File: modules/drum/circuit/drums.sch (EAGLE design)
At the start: 43 parts, among them IC1 LM324N, IC2 LM324N, Q1 2N3904

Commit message: a few misc changes
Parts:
- added 10K_POT5, 10K_POT6, 10K_POT7, HH_TRIGGER, WOODBLOCK_TRIGGER: (no value), pinhead:PINHD-1X2
- added 1M: 1M, SparkFun-Resistors:100KOHM-HORIZ-1/4W-5%
- added C10, C9: 6800pF, capacitor-wima:C5/3
- added C11: 10uF, rcl:CPOL-USTT5D11
- added C12: 0.1uF, capacitor-wima:C5/3
- added C13, C14: 100pF, capacitor-wima:C5/3
- added C15: 4.7nF, capacitor-wima:C5/3
- added C16, C17: 300pF, capacitor-wima:C5/3
- added D3, D4, D5: 1A/50V/1.1V, SparkFun-DiscreteSemi:DIODE-KIT2
- added FTDI: (no value), pinhead:PINHD-1X6
- added JP1: (no value), pinhead:PINHD-1X4
- added Q2: 2N3904, transistor-small-signal:2N3904
- added R22: 100k, SparkFun-Resistors:100KOHM-HORIZ-1/4W-5%
- added R23, R27: 1k, SparkFun-Resistors:100KOHM-HORIZ-1/4W-5%
- added R24: 2M, SparkFun-Resistors:100KOHM-HORIZ-1/4W-5%
- added R25: 10k, SparkFun-Resistors:100KOHM-HORIZ-1/4W-5%
- added R26, R28, R29, R36: 100, SparkFun-Resistors:100KOHM-HORIZ-1/4W-5%
- added R30, R37: 100K, SparkFun-Resistors:100KOHM-HORIZ-1/4W-5%
- added R31: 50K, SparkFun-Resistors:100KOHM-HORIZ-1/4W-5%
- added R32: 3.6K, SparkFun-Resistors:100KOHM-HORIZ-1/4W-5%
- added R33: 10K, SparkFun-Resistors:100KOHM-HORIZ-1/4W-5%
- added R34, R35: 220K, SparkFun-Resistors:100KOHM-HORIZ-1/4W-5%
- C4: value 10uF -> 0.1uF
- R10: value 50K -> 100K
- R9: value 100K -> 50K
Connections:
- removed net N$15: IC1B.-IN, R10.2, R9.1
- removed net N$5: C3.2, IC1A.OUT, R10.1, R3.2, R5.2
- new net +12V: JP1.1
- new net -5V: IC1P.V-, IC2P.V-
- new net HH_OUT: C17.2, IC1D.OUT, R35.1, R37.1
- new net N$25: D3.A, WOODBLOCK_TRIGGER.2
- new net N$26: D3.C, R22.1
- new net N$27: IC1C.+IN, R22.2, R23.2
- new net N$29: 10K_POT5.1, C10.1, C9.2, R27.2
- new net N$30: C9.1, IC1C.-IN, R24.1
- new net N$31: 10K_POT5.2, R27.1, R28.2
- new net N$32: D4.A, HH_TRIGGER.2
- new net N$33: C11.+, D4.C, R26.2
- new net N$34: IC2C.+IN, R10.2, R30.1, R31.2, R37.2, R9.2
- new net N$35: 10K_POT6.1, R26.1
- new net N$36: 10K_POT6.2, C15.1, D5.A
- new net N$37: C4.2, NOISE_CHIP.(PCINT11/~RESET/DW)PB3, R25.1
- new net N$38: D5.C, Q2.C
- new net N$39: C12.1, R32.1
- new net N$40: 1M.2, C12.2, C13.2, Q2.B
- new net N$41: HH_TRIGGER.1, R29.2
- new net N$42: C13.1, R33.1
- new net N$43: C15.2, R34.2
- new net N$44: C14.2, R32.2
- new net N$45: 10K_POT7.1, R36.2
- new net N$46: C16.2, C17.1, R36.1
- new net N$48: C16.1, IC1D.-IN, R34.1, R35.2
- new net OUT: IC2C.OUT, JP1.4, R30.2
- new net RESET: C4.1, FTDI.6
- new net RX: FTDI.5, NOISE_CHIP.(PCINT1/AIN0/ADC1)PA1
- new net TX: FTDI.4, NOISE_CHIP.(PCINT2/AIN1/ADC2)PA2
- new net WB_OUT: C10.2, IC1C.OUT, R24.2, R9.1
- net +5V: now also 1M.1, IC1P.V+, IC2P.V+, R25.2, R29.1, WOODBLOCK_TRIGGER.1
- net BD_OUT: now also C3.2, IC1A.OUT, R3.2, R31.1, R5.2; no longer IC1B.OUT, R9.2
- net GND: now also 10K_POT7.2, C11.-, FTDI.1, IC1D.+IN, IC2C.-IN, JP1.3, Q2.E, R23.1, R28.1; no longer IC1B.+IN
- net METALIC: now also C14.1
- net NOISE: now also R33.2
- net SNARE_OUT: now also R10.1
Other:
- moved on the sheet: 10K_POT, 10K_POT1, 10K_POT2, 10K_POT3, BD_TRIGGER, IC1A, IC1C, IC1D, IC2A, IC2B, IC2C, IC2D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

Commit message: Drums
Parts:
- removed METAL_POT: metal_pot, pinhead:PINHD-1X3
- added 1M1, 1M2: 220, SparkFun-Resistors:100KOHM-HORIZ-1/4W-5%
- added C18, C19, C20: 100nF, capacitor-wima:C5/3
- added D6: 1A/50V/1.1V, SparkFun-DiscreteSemi:DIODE-KIT2
- added OK1: 6N138, optocoupler:6N138
- added R38, R39, R41, R42, R43, R44, R45: 100k, SparkFun-Resistors:100KOHM-HORIZ-1/4W-5%
- added R40: 10k, SparkFun-Resistors:100KOHM-HORIZ-1/4W-5%
- R11: value 100k -> 100
- R12, R23: value 1k -> 100k
- R19: value 100K -> 100k
- R2: value 1k -> 10k
- R20: value 50K -> 100k
- R21: value 100K -> 100
- R22: value 100k -> 10k
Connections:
- removed net N$1: METAL_POT.2, NOISE_CHIP.(PCINT5/OC1B/MISO/DO/ADC5)PA5
- removed net N$13: IC2A.+IN, R11.2, R12.2
- removed net N$14: C7.2, IC2A.OUT, R13.2, R15.2, R20.1
- removed net N$21: IC2B.-IN, R19.1, R20.2
- removed net N$8: D2.A, SNARE_TRIGGER.2
- new net BD_TRIGGER: NOISE_CHIP.(PCINT8/XTAL1/CLKI)PB0, R12.2
- new net DIN5_4: 1M2.2
- new net DIN5_5: D2.A, OK1.C
- new net HH_TRIGGER: NOISE_CHIP.(PCINT10/INT0/OC0A/CKOUT)PB2, R11.2
- new net MIDI_RX: 1M1.1, NOISE_CHIP.(PCINT6/OC1A/SDA/MOSI/ADC6)PA6, OK1.VO
- new net N$15: C19.1, R19.1, R42.2, WOODBLOCK_TRIGGER.2
- new net N$28: D6.C, IC1C.+IN, R40.2
- new net N$47: R41.2, WOODBLOCK_TRIGGER.1
- new net N$49: C19.2, D6.A, R43.2
- new net N$5: BD_TRIGGER.1, R38.2
- new net N$50: C20.2, D3.A, R45.2
- new net SNARE_TRIGGER: NOISE_CHIP.(PCINT0/AREF/ADC0)PA0, R20.2
- new net WB_TRIGGER: NOISE_CHIP.(PCINT9/XTAL2)PB1, R19.2
- net +5V: now also 1M1.2, OK1.VCC, R23.1, R38.1, R41.1; no longer BD_TRIGGER.1, METAL_POT.1, SNARE_TRIGGER.1, WOODBLOCK_TRIGGER.1
- net BD_OUT: now also C7.2, IC2A.OUT, R13.2, R15.2; no longer IC2B.OUT, R19.2
- net GND: now also OK1.GND, R1.1, R22.1, R39.1, R40.1, R42.1, R43.1, R44.1, R45.1; no longer IC2B.+IN, METAL_POT.3, R12.1, R23.1
- net N$12: now also 1M2.1, OK1.A; no longer R11.1
- net N$2: now also C18.1, R12.1, R39.2; no longer D1.A
- net N$25: now also C20.1, R20.1, R44.2, SNARE_TRIGGER.2; no longer D3.A, WOODBLOCK_TRIGGER.2
- net N$26: now also IC2A.+IN, R22.2; no longer R22.1
- net N$27: now also SNARE_TRIGGER.1; no longer IC1C.+IN, R22.2
- net N$3: now also IC1A.+IN, R2.2; no longer R1.1
- net N$32: now also R11.1
- net N$4: now also C18.2, D1.A; no longer IC1A.+IN, R2.2
- net NOISE: now also NOISE_CHIP.(PCINT5/OC1B/MISO/DO/ADC5)PA5; no longer NOISE_CHIP.(PCINT6/OC1A/SDA/MOSI/ADC6)PA6
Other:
- moved on the sheet: BD_TRIGGER, SNARE_TRIGGER, WOODBLOCK_TRIGGER

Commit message: drum board
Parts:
- added 10K_POT8, 10K_POT9, CLING_TRIGGER: (no value), pinhead:PINHD-1X2
- added 1M3, 1M4, R49: 1k, SparkFun-Resistors:100KOHM-HORIZ-1/4W-5%
- added C21, C22, C24, C26, C28: 100nF, capacitor-wima:C5/3
- added C23: 10uF, rcl:CPOL-USTT5D11
- added C25, C27: 330nF, capacitor-wima:C5/3
- added D7, D8: 1A/50V/1.1V, SparkFun-DiscreteSemi:DIODE-KIT2
- added IC3: 7905, linear:7905T
- added IC4: 7805T, adafruit:7805T
- added Q3: 2N3904, transistor-small-signal:2N3904
- added R46: 1M, SparkFun-Resistors:100KOHM-HORIZ-1/4W-5%
- added R47, R48: 47K, SparkFun-Resistors:100KOHM-HORIZ-1/4W-5%
- added R50: 100, SparkFun-Resistors:100KOHM-HORIZ-1/4W-5%
- added R51: 2.2K, SparkFun-Resistors:100KOHM-HORIZ-1/4W-5%
- added R52, R54, R55, R56, R57: 100k, SparkFun-Resistors:100KOHM-HORIZ-1/4W-5%
- added R53, R59: 10k, SparkFun-Resistors:100KOHM-HORIZ-1/4W-5%
- added R58: 100K, SparkFun-Resistors:100KOHM-HORIZ-1/4W-5%
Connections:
- new net 10K_POT3: 10K_POT9.1, R47.1, R48.1
- new net BD_OUT1: C22.2, IC2B.OUT, R46.2, R48.2, R59.2
- new net CLING_OUT: IC1B.-IN, IC1B.OUT, R58.1
- new net CLING_TRIGGER: NOISE_CHIP.(PCINT3/T0/ADC3)PA3, R57.2
- new net GND2: 1M4.1, C27.1, IC3.VI, JP1.3
- new net N$1: 10K_POT8.1, C21.2, C22.1, R49.2
- new net N$13: 10K_POT8.2, R49.1, R50.2
- new net N$14: 10K_POT9.2, R51.1
- new net N$21: C23.+, R51.2
- new net N$51: Q3.B, R52.2
- new net N$52: D8.C, Q3.C
- new net N$53: D8.A, IC1B.+IN, R59.1
- new net N$54: C24.1, CLING_TRIGGER.2, R55.2, R57.1
- new net N$55: D7.C, IC2B.+IN, R53.2
- new net N$56: CLING_TRIGGER.1, R54.2
- new net N$57: C24.2, D7.A, R56.2
- new net N$8: C21.1, IC2B.-IN, R46.1, R47.2
- net +12V: now also 1M3.2, C25.2, IC4.VI
- net +5V: now also C26.2, IC4.VO, R54.1
- net -5V: now also C28.1, IC3.VO
- net GND: now also 1M3.1, 1M4.2, C23.-, C25.1, C26.1, C27.2, C28.2, IC3.GND, IC4.GND, Q3.E, R50.1, R53.1, R55.1, R56.1; no longer JP1.3
- net METALIC: now also R52.1
- net N$34: now also R58.2

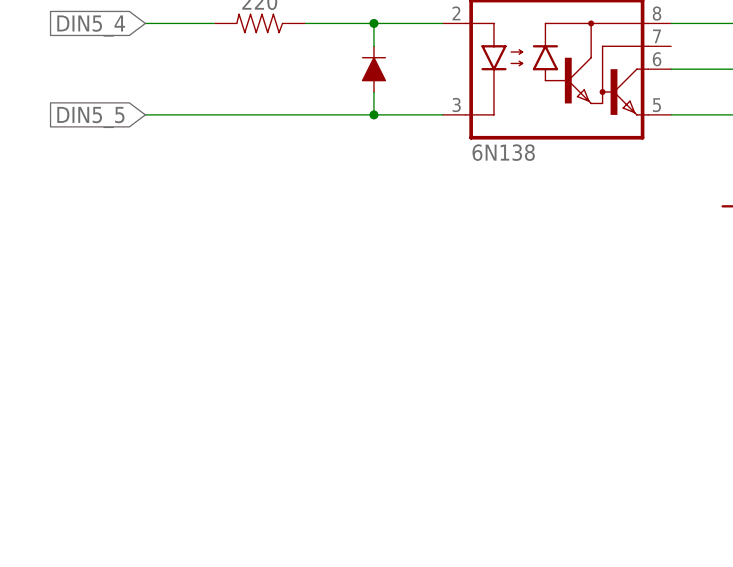
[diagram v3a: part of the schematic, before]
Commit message: drum board cleanup
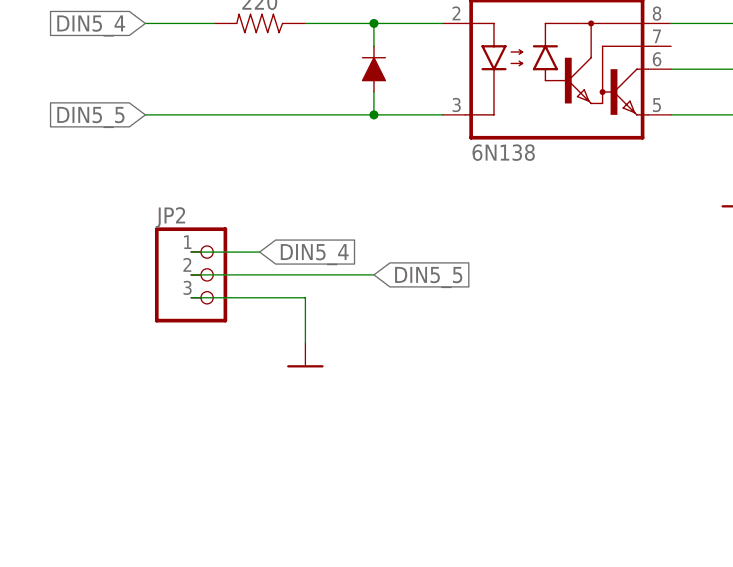
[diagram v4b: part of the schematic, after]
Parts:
- added JP2: (no value), adafruit:PINHD-1X3
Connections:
- net DIN5_4: now also JP2.1
- net DIN5_5: now also JP2.2
- net GND: now also JP2.3
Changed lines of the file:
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@@
 <?xml version="1.0" encoding="utf-8"?>
 <!DOCTYPE eagle SYSTEM "eagle.dtd">
-<eagle version="9.6.2">
+<eagle version="9.5.2">
 <drawing>
 <settings>
@@
 <part name="R59" library="SparkFun-Resistors" library_urn="urn:adsk.eagle:library:532" deviceset="100KOHM" device="-HORIZ-1/4W-5%" package3d_urn="urn:adsk.eagle:package:39658/1" value="10k"/>
 <part name="D8" library="SparkFun-DiscreteSemi" library_urn="urn:adsk.eagle:library:514" deviceset="DIODE" device="-KIT2" package3d_urn="urn:adsk.eagle:package:38455/1" value="1A/50V/1.1V"/>
+<part name="JP2" library="adafruit" library_urn="urn:adsk.eagle:library:420" deviceset="PINHD-1X3" device="" package3d_urn="urn:adsk.eagle:package:6240710/1"/>
+<part name="GND31" library="supply1" library_urn="urn:adsk.eagle:library:371" deviceset="GND" device=""/>
 </parts>
 <sheets>
@@
 </instance>
 <instance part="D8" gate="G$1" x="574.04" y="-294.64" smashed="yes" rot="R270"/>
+<instance part="JP2" gate="A" x="63.5" y="-101.6" smashed="yes">
+<attribute name="NAME" x="57.15" y="-95.885" size="1.778" layer="95"/>
+<attribute name="VALUE" x="57.15" y="-109.22" size="1.778" layer="96"/>
+</instance>
+<instance part="GND31" gate="1" x="73.66" y="-111.76" smashed="yes"/>
 </instances>
 <busses>
@@
 <wire x1="127" y1="-177.8" x2="127" y2="-172.72" width="0.1524" layer="91"/>
 </segment>
+<segment>
+<pinref part="JP2" gate="A" pin="3"/>
+<wire x1="60.96" y1="-104.14" x2="73.66" y2="-104.14" width="0.1524" layer="91"/>
+<wire x1="73.66" y1="-104.14" x2="73.66" y2="-109.22" width="0.1524" layer="91"/>
+<pinref part="GND31" gate="1" pin="GND"/>
+</segment>
 </net>
 <net name="METALIC" class="0">
@@
 <label x="55.88" y="-73.66" size="1.778" layer="95" rot="R180" xref="yes"/>
 </segment>
+<segment>
+<pinref part="JP2" gate="A" pin="1"/>
+<wire x1="60.96" y1="-99.06" x2="68.58" y2="-99.06" width="0.1524" layer="91"/>
+<label x="68.58" y="-99.06" size="1.778" layer="95" xref="yes"/>
+</segment>
 </net>
 <net name="N$12" class="0">
@@
 <label x="55.88" y="-83.82" size="1.778" layer="95" rot="R180" xref="yes"/>
 </segment>
-</net>
+<segment>
+<pinref part="JP2" gate="A" pin="2"/>
+<wire x1="60.96" y1="-101.6" x2="81.28" y2="-101.6" width="0.1524" layer="91"/>
+<label x="81.28" y="-101.6" size="1.778" layer="95" xref="yes"/>
+</segment>
+</net>

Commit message: drum machine
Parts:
- removed 1M3, 1M4: 1k, SparkFun-Resistors:100KOHM-HORIZ-1/4W-5%
- removed C25, C27: 330nF, capacitor-wima:C5/3
- removed C26, C28: 100nF, capacitor-wima:C5/3
- removed IC3: 7905, linear:7905T
- removed IC4: 7805T, adafruit:7805T
- removed JP1: (no value), pinhead:PINHD-1X4
- added JP3: (no value), pinhead:PINHD-1X6
- added LIMIT_SWITCH, LIM_SWITCH1, LOW_BIT_NOISE: (no value), pinhead:PINHD-1X2
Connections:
- removed net -5V: C28.1, IC1P.V-, IC2P.V-, IC3.VO
- removed net GND2: 1M4.1, C27.1, IC3.VI, JP1.3
- new net -12V: IC1P.V-, IC2P.V-, JP3.2
- new net N$58: LIM_SWITCH1.2, R6.2
- new net N$59: LIMIT_SWITCH.2, R49.2
- new net N$60: LOW_BIT_NOISE.1, NOISE_CHIP.(PCINT4/T1/SCL/USCK/ADC4)PA4
- net +12V: now also IC1P.V+, IC2P.V+, JP3.1; no longer 1M3.2, C25.2, IC4.VI, JP1.1
- net +5V: now also JP3.6; no longer C26.2, IC1P.V+, IC2P.V+, IC4.VO
- net GND: now also JP3.3, LOW_BIT_NOISE.2; no longer 1M3.1, 1M4.2, C25.1, C26.1, C27.2, C28.2, IC3.GND, IC4.GND
- net N$1: now also LIMIT_SWITCH.1; no longer R49.2
- net N$6: now also LIM_SWITCH1.1; no longer R6.2
- net OUT: now also JP3.4; no longer JP1.4

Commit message: long overdue commit
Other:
- moved on the sheet: FTDI, JP2, JP3, LOW_BIT_NOISE, NOISE_CHIP, OK1
